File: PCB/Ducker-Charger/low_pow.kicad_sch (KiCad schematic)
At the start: 54 parts, among them IC1 STUSB4710AQ1TR, J3 Conn_01x02, J4 USB_A, J5 USB_A, Q10 AO3400A, Q11 AO3400A, Q6 AO4407A, Q7 AO3400A, Q8 AO4407A, Q9 AO3400A, U3 STPD01PUR, U4 TPS54302, U5 INA3221, U6 TPS54302

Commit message: feat: updated footprints
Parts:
- C16, C17, C18, C19, C21, C22, C23, C25, C26, C27, CCDC1, Cin1, Cout1, Cout2: footprint (none) -> Capacitor_SMD:C_0805_2012Metric
- C20, C24, CBOOT1: footprint (none) -> Capacitor_SMD:C_0603_1608Metric
- IC1: footprint QFN50P300X300X65-16N -> Package_DFN_QFN:QFN-16-1EP_3x3mm_P0.5mm_EP1.7x1.7mm
- J4, J5: footprint (none) -> Connector_USB:USB_A_Molex_67643_Horizontal
- L2: footprint (none) -> Inductor_SMD:L_6.3x6.3_H3
- L3, L4: footprint (none) -> Inductor_SMD:L_7.3x7.3_H4.5
- R12, R13, R14, R15, R16, R17, R18, R19, R20, R21, R22, R23, R24, R25, RCDC1, Ron1, Rshunt1, Rshunt2, Rsns1: footprint (none) -> Resistor_SMD:R_0603_1608Metric
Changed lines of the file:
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@@
 			)
 		)
-		(property "Footprint" ""
+		(property "Footprint" "Resistor_SMD:R_0603_1608Metric"
 			(at 207.518 102.87 90)
 			(effects
@@
 			)
 		)
-		(property "Footprint" ""
+		(property "Footprint" "Resistor_SMD:R_0603_1608Metric"
 			(at 121.92 180.848 90)
 			(effects
@@
 			)
 		)
-		(property "Footprint" ""
+		(property "Footprint" "Resistor_SMD:R_0603_1608Metric"
 			(at 196.85 109.728 90)
 			(effects
@@
 			)
 		)
-		(property "Footprint" ""
+		(property "Footprint" "Capacitor_SMD:C_0805_2012Metric"
 			(at 270.2052 96.52 0)
 			(effects
@@
 			)
 		)
-		(property "Footprint" ""
+		(property "Footprint" "Capacitor_SMD:C_0805_2012Metric"
 			(at 277.8252 218.44 0)
 			(effects
@@
 			)
 		)
-		(property "Footprint" ""
+		(property "Footprint" "Resistor_SMD:R_0603_1608Metric"
 			(at 328.93 212.598 90)
 			(effects
@@
 			)
 		)
-		(property "Footprint" ""
+		(property "Footprint" "Inductor_SMD:L_7.3x7.3_H4.5"
 			(at 269.24 179.07 0)
 			(effects
@@
 			)
 		)
-		(property "Footprint" ""
+		(property "Footprint" "Capacitor_SMD:C_0805_2012Metric"
 			(at 204.1652 217.17 0)
 			(effects
@@
 			)
 		)
-		(property "Footprint" ""
+		(property "Footprint" "Connector_USB:USB_A_Molex_67643_Horizontal"
 			(at 350.52 217.17 0)
 			(effects
@@
 			)
 		)
-		(property "Footprint" ""
+		(property "Footprint" "Capacitor_SMD:C_0805_2012Metric"
 			(at 287.9852 186.69 0)
 			(effects
@@
 			)
 		)
-		(property "Footprint" ""
+		(property "Footprint" "Capacitor_SMD:C_0805_2012Metric"
 			(at 58.1152 80.01 0)
 			(effects
@@
 			)
 		)
-		(property "Footprint" ""
+		(property "Footprint" "Capacitor_SMD:C_0805_2012Metric"
 			(at 117.8052 77.47 0)
 			(effects
@@
 			)
 		)
-		(property "Footprint" ""
+		(property "Footprint" "Capacitor_SMD:C_0603_1608Metric"
 			(at 260.0452 210.82 0)
 			(effects
@@
 			)
 		)
-		(property "Footprint" ""
+		(property "Footprint" "Capacitor_SMD:C_0805_2012Metric"
 			(at 258.7752 96.52 0)
 			(effects
@@
 			)
 		)
-		(property "Footprint" ""
+		(property "Footprint" "Capacitor_SMD:C_0603_1608Metric"
 			(at 100.0252 82.55 0)
 			(effects
@@
 			)
 		)
-		(property "Footprint" ""
+		(property "Footprint" "Resistor_SMD:R_0603_1608Metric"
 			(at 196.85 74.168 90)
 			(effects
@@
 			)
 		)
-		(property "Footprint" ""
+		(property "Footprint" "Capacitor_SMD:C_0805_2012Metric"
 			(at 202.8952 185.42 0)
 			(effects
@@
 			)
 		)
-		(property "Footprint" ""
+		(property "Footprint" "Resistor_SMD:R_0603_1608Metric"
 			(at 99.06 74.168 90)
 			(effects
@@
 			)
 		)
-		(property "Footprint" ""
+		(property "Footprint" "Resistor_SMD:R_0603_1608Metric"
 			(at 327.66 180.848 90)
 			(effects
@@
 			)
 		)
-		(property "Footprint" ""
+		(property "Footprint" "Resistor_SMD:R_0603_1608Metric"
 			(at 123.19 212.598 90)
 			(effects
@@
 			)
 		)
-		(property "Footprint" ""
+		(property "Footprint" "Capacitor_SMD:C_0805_2012Metric"
 			(at 289.2552 218.44 0)
 			(effects
@@
 			)
 		)
-		(property "Footprint" ""
+		(property "Footprint" "Connector_USB:USB_A_Molex_67643_Horizontal"
 			(at 349.25 185.42 0)
 			(effects
@@
 			)
 		)
-		(property "Footprint" ""
+		(property "Footprint" "Resistor_SMD:R_0603_1608Metric"
 			(at 132.842 66.04 90)
 			(effects
@@
 			)
 		)
-		(property "Footprint" ""
+		(property "Footprint" "Resistor_SMD:R_0603_1608Metric"
 			(at 128.778 184.15 90)
 			(effects
@@
 			)
 		)
-		(property "Footprint" ""
+		(property "Footprint" "Resistor_SMD:R_0603_1608Metric"
 			(at 316.23 62.738 90)
 			(effects
@@
 			)
 		)
-		(property "Footprint" ""
+		(property "Footprint" "Resistor_SMD:R_0603_1608Metric"
 			(at 207.518 67.31 90)
 			(effects
@@
 			)
 		)
-		(property "Footprint" ""
+		(property "Footprint" "Capacitor_SMD:C_0805_2012Metric"
 			(at 144.4752 69.85 0)
 			(effects
@@
 			)
 		)
-		(property "Footprint" ""
+		(property "Footprint" "Resistor_SMD:R_0603_1608Metric"
 			(at 127 84.328 90)
 			(effects
@@
 			)
 		)
-		(property "Footprint" ""
+		(property "Footprint" "Resistor_SMD:R_0603_1608Metric"
 			(at 295.402 194.31 90)
 			(effects
@@
 			)
 		)
-		(property "Footprint" ""
+		(property "Footprint" "Resistor_SMD:R_0603_1608Metric"
 			(at 296.672 214.63 90)
 			(effects
@@
 			)
 		)
-		(property "Footprint" ""
+		(property "Footprint" "Inductor_SMD:L_6.3x6.3_H3"
 			(at 106.68 82.55 0)
 			(effects
@@
 			)
 		)
-		(property "Footprint" ""
+		(property "Footprint" "Resistor_SMD:R_0603_1608Metric"
 			(at 295.402 182.88 90)
 			(effects
@@
 			)
 		)
-		(property "Footprint" ""
+		(property "Footprint" "Capacitor_SMD:C_0603_1608Metric"
 			(at 258.7752 179.07 0)
 			(effects
@@
 			)
 		)
-		(property "Footprint" ""
+		(property "Footprint" "Capacitor_SMD:C_0805_2012Metric"
 			(at 35.8648 74.93 0)
 			(effects
@@
 			)
 		)
-		(property "Footprint" ""
+		(property "Footprint" "Capacitor_SMD:C_0805_2012Metric"
 			(at 115.2652 90.17 0)
 			(effects
@@
 			)
 		)
-		(property "Footprint" ""
+		(property "Footprint" "Resistor_SMD:R_0603_1608Metric"
 			(at 316.23 65.278 90)
 			(effects
@@
 			)
 		)
-		(property "Footprint" ""
+		(property "Footprint" "Resistor_SMD:R_0603_1608Metric"
 			(at 130.048 215.9 90)
 			(effects
@@
 			)
 		)
-		(property "Footprint" ""
+		(property "Footprint" "Inductor_SMD:L_7.3x7.3_H4.5"
 			(at 270.51 210.82 0)
 			(effects
@@
 			)
 		)
-		(property "Footprint" ""
+		(property "Footprint" "Capacitor_SMD:C_0805_2012Metric"
 			(at 276.5552 186.69 0)
 			(effects
@@
 			)
 		)
-		(property "Footprint" ""
+		(property "Footprint" "Capacitor_SMD:C_0805_2012Metric"
 			(at 139.3952 90.17 0)
 			(effects
@@
 			)
 		)
-		(property "Footprint" "QFN50P300X300X65-16N"
+		(property "Footprint" "Package_DFN_QFN:QFN-16-1EP_3x3mm_P0.5mm_EP1.7x1.7mm"
 			(at 306.07 150.8 0)
 			(effects
@@
 			)
 		)
-		(property "Footprint" ""
+		(property "Footprint" "Resistor_SMD:R_0603_1608Metric"
 			(at 296.672 226.06 90)
 			(effects

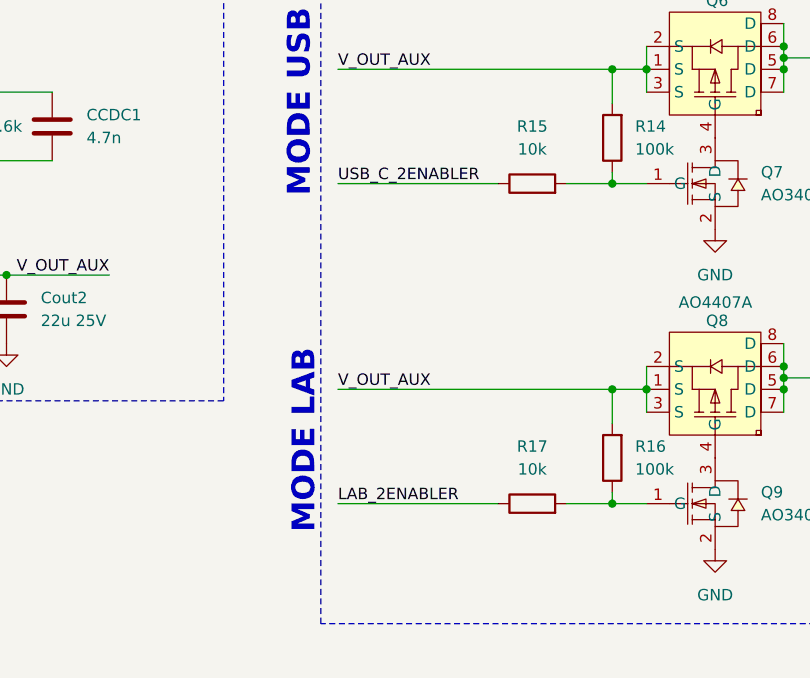
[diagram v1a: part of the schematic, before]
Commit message: fix: updated config based on CubeMX
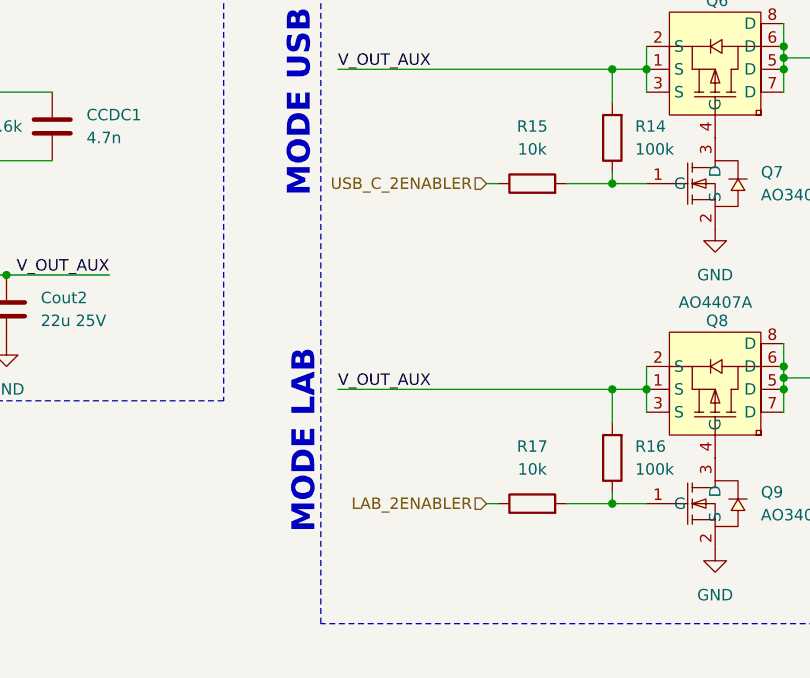
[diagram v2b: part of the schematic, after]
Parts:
- Rsns1: footprint Resistor_SMD:R_0603_1608Metric -> Resistor_SMD:R_1206_3216Metric
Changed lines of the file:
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@@
 	(wire
 		(pts
-			(xy 44.45 274.32) (xy 58.42 274.32)
+			(xy 191.77 107.95) (xy 193.04 107.95)
 		)
 		(stroke
@@
 	(wire
 		(pts
-			(xy 52.07 59.69) (xy 64.77 59.69)
+			(xy 44.45 274.32) (xy 58.42 274.32)
 		)
 		(stroke
@@
 	(wire
 		(pts
-			(xy 236.22 93.98) (xy 224.79 93.98)
+			(xy 52.07 59.69) (xy 64.77 59.69)
 		)
 		(stroke
@@
 	(wire
 		(pts
-			(xy 175.26 72.39) (xy 193.04 72.39)
+			(xy 236.22 93.98) (xy 224.79 93.98)
 		)
 		(stroke
@@
 	(wire
 		(pts
+			(xy 191.77 72.39) (xy 193.04 72.39)
+		)
+		(stroke
+			(width 0)
+			(type default)
+		)
+	)
+	(wire
+		(pts
 			(xy 359.41 81.28) (xy 370.84 81.28)
 		)
@@
 	(wire
 		(pts
-			(xy 175.26 107.95) (xy 193.04 107.95)
-		)
-		(stroke
-			(width 0)
-			(type default)
-		)
-	)
-	(wire
-		(pts
 			(xy 175.26 59.69) (xy 205.74 59.69)
 		)
@@
 		)
 	)
-	(label "LAB_2ENABLER"
-		(at 175.26 107.95 0)
-		(effects
-			(font
-				(size 1.27 1.27)
-			)
-			(justify left bottom)
-		)
-	)
 	(label "USB_A1_FB"
 		(at 309.88 187.96 180)
@@
 		)
 	)
-	(label "USB_C_2ENABLER"
-		(at 175.26 72.39 0)
-		(effects
-			(font
-				(size 1.27 1.27)
-			)
-			(justify left bottom)
-		)
-	)
 	(label "I2C_LP.SDA"
 		(at 86.36 200.66 180)
@@
 		)
 	)
+	(hierarchical_label "USB_C_2ENABLER"
+		(shape input)
+		(at 191.77 72.39 180)
+		(effects
+			(font
+				(size 1.27 1.27)
+			)
+			(justify right)
+		)
+	)
+	(hierarchical_label "LAB_2ENABLER"
+		(shape input)
+		(at 191.77 107.95 180)
+		(effects
+			(font
+				(size 1.27 1.27)
+			)
+			(justify right)
+		)
+	)
 	(symbol
 		(lib_id "power:GND")
@@
 			)
 		)
-		(property "Footprint" "Resistor_SMD:R_0603_1608Metric"
+		(property "Footprint" "Resistor_SMD:R_1206_3216Metric"
 			(at 127 84.328 90)
 			(effects

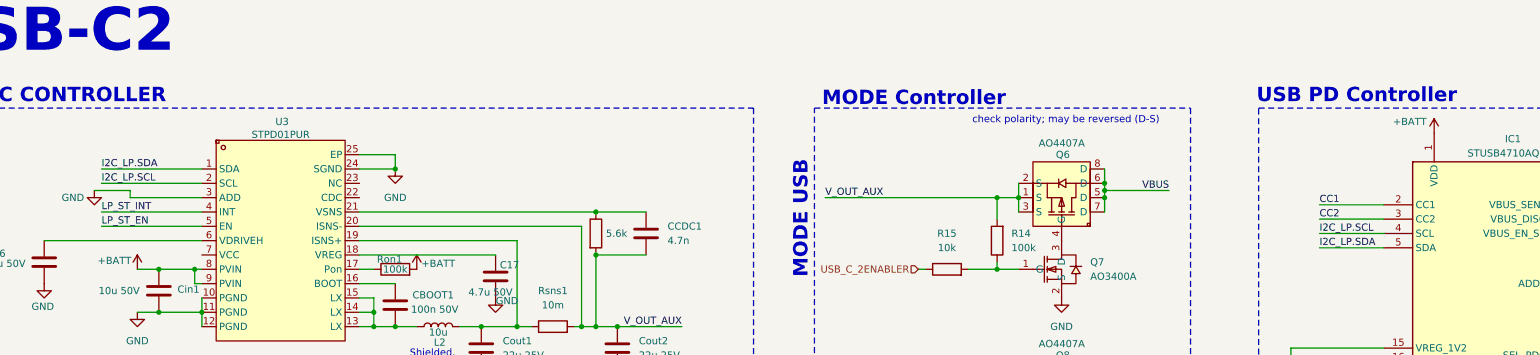
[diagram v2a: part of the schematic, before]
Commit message: fix: added missing connections
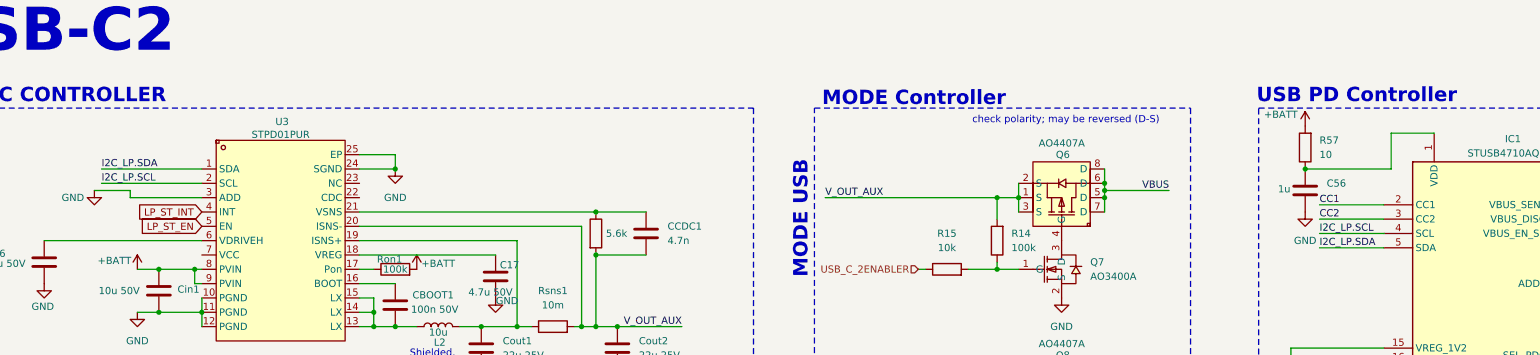
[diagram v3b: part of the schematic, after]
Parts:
- added C56: 1u, Capacitor_SMD:C_0603_1608Metric, symbol Device:C
- added R57: 10, Resistor_SMD:R_0603_1608Metric, symbol Device:R
- Rshunt1, Rshunt2: footprint Resistor_SMD:R_0603_1608Metric -> Resistor_SMD:R_1206_3216Metric
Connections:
- net +BATT: now also R57.2; no longer IC1.1 (VDD)
- net GND: now also C56.2
- new net: C56.1, IC1.1 (VDD), R57.1

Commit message: feat: remade the PCB & minor schematic fixes
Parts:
- added D301: USBLC6-4SC6, EasyEDA:SOT-23-6_L2.9-W1.6-P0.95-LS2.8-BL, symbol EasyEDA:USBLC6-4SC6
- added R309, R310, RCDC301: 10k, Resistor_SMD:R_0603_1608Metric, symbol Device:R
- C303: renamed from C21; value 10u -> 10u 25V; footprint Capacitor_SMD:C_0805_2012Metric -> Capacitor_SMD:C_1206_3216Metric
- C304: renamed from C25; value 10u -> 10u 25V; footprint Capacitor_SMD:C_0805_2012Metric -> Capacitor_SMD:C_1206_3216Metric
- Cout301: renamed from Cout1; value 22u 25V -> 22u 35V; footprint Capacitor_SMD:C_0805_2012Metric -> Capacitor_SMD:C_1210_3225Metric
- Cout302: renamed from Cout2; value 22u 25V -> 22u 35V; footprint Capacitor_SMD:C_0805_2012Metric -> Capacitor_SMD:C_1210_3225Metric
- J303: renamed from J3; footprint (none) -> TerminalBlock:TerminalBlock_bornier-2_P5.08mm
- L301: renamed from L2; value 10u -> 10u 5A; footprint Inductor_SMD:L_6.3x6.3_H3 -> Inductor_SMD:L_7.3x7.3_H4.5
- Rsns301: renamed from Rsns1; value 10m -> 25m
- renumbered C16 to C301, C17 to C302, C18 to C305, C20 to C306, C24 to C307, C56 to C308, C19 to C309, C22 to C310, C26 to C311, C23 to C312, C27 to C313, CBOOT1 to CBOOT301, CCDC1 to CCDC301, Cin1 to Cin301, IC1 to IC301, J4 to J301, J5 to J302, L3 to L302, L4 to L303, Q10 to Q301, Q11 to Q302, Q7 to Q303, Q9 to Q304, Q6 to Q305, Q8 to Q306, R18 to R301, R22 to R302, R20 to R303, R24 to R304, R15 to R305, R17 to R306, R14 to R307, R16 to R308, R57 to R311, R19 to R312, R21 to R313, R23 to R314, R25 to R315, R12 to R316, R13 to R317, RCDC1 to RCDC302, Ron1 to Ron301, Rshunt1 to Rshunt301, Rshunt2 to Rshunt302, U5 to U301, U3 to U302, U4 to U303, U6 to U304, USBC2 to USBC301
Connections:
- net +3V3: now also R309.1, R310.1
- net +BATT: now also U302.7 (VCC); no longer Ron301.2
- net CC1: now also D301.4
- net CC2: now also D301.6
- net DN: now also D301.3
- net DP: now also D301.1
- net GND: now also U301.1 (IN-3), U301.2 (IN+3), D301.2, RCDC301.2
- net USB_A1_EN: now also R309.2
- net USB_A2_EN: now also R310.2
- net VBUS: now also D301.5
- net at U302.22 (CDC): now also RCDC301.1
- net C2_RDY renamed C2.RDY
- net LAB_2ENABLER renamed C2.LAB_EN
- net LP_ST_EN renamed C2.ST_EN
- net LP_ST_INT renamed C2.ST_INT
- net USB_A1_CTRL renamed USBA.1_CTRL
- net USB_A2_CTRL renamed USBA.2_CTRL
- net USB_C_2ENABLER renamed C2.PORT_EN
- new net +5V: Ron301.2
- no-connect marks 4 -> 12
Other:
- note added: "ESD PROTECTION"
- moved on the sheet: C301, C302, C305, C308, C309, CBOOT301, CCDC301, Cin301, Cout301, Cout302, IC301, J303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

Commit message: feat: final version before prod
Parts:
- removed IC301: STUSB4710AQ1TR, Package_DFN_QFN:QFN-16-1EP_3x3mm_P0.5mm_EP1.7x1.7mm, symbol STUSB4710AQ1TR:STUSB4710AQ1TR
- removed R317: 50, Resistor_SMD:R_0603_1608Metric, symbol Device:R
- added C314: 1u, Resistor_SMD:R_0603_1608Metric, symbol Device:C
- added C327: 2.2u, Capacitor_SMD:C_0805_2012Metric, symbol Device:C
- added C391: 100n, Resistor_SMD:R_0603_1608Metric, symbol Device:C
- added D302: LED, LED_SMD:LED_0603_1608Metric, symbol Device:LED
- added IC302: CYPD3175-24LQXQ, QFN50P400X400X60-25N-D, symbol LIB_CYPD3175-24LQXQ:CYPD3175-24LQXQ
- added J304: Debug, Eagle_Connectors:SAMTEC_FTSH-107-01-L-DV-K-TR, symbol Connector:Conn_ST_STDC14
- added R318: 1k, Resistor_SMD:R_0603_1608Metric, symbol Device:R
- C305: value 1u -> 390p; footprint Capacitor_SMD:C_0805_2012Metric -> Resistor_SMD:R_0603_1608Metric
- C308: value 1u -> 390p; footprint Capacitor_SMD:C_0603_1608Metric -> Resistor_SMD:R_0603_1608Metric
- C309: value 1u -> 100n; footprint Capacitor_SMD:C_0805_2012Metric -> Resistor_SMD:R_0603_1608Metric
- R311: value 10 -> 200k
- R316: value 1k2 -> 63k
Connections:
- net +3V3: now also C327.1, C391.1, IC302.23 (VDDD), J304.3 (VCC)
- net +BATT: no longer R311.2
- net C2.RDY: now also IC302.10 (GPIO_3)
- net CC1: now also C305.1, IC302.15 (CC1)
- net CC2: now also C308.1, IC302.14 (CC2)
- net GND: now also R316.2, C314.2, C327.2, C391.2, D302.1 (K), IC302.22 (GND), IC302.25 (EPAD), J304.11 (GNDDetect), J304.5 (GND), J304.7 (GND)
- net I2C_LP.SCL: now also IC302.13 (GPIO_20VT_2)
- net I2C_LP.SDA: now also IC302.12 (GPIO_20VT_1)
- net VBUS: now also R311.1, IC302.11 (VBUS_C_MON_DISCH), IC302.19 (CSP); no longer R316.2
- net at C309.1: now also IC302.21 (CATH/COMP)
- net at R316.1: now also R311.2, IC302.20 (FB)
- new net: D302.2 (A), R318.2
- new net: C314.1, IC302.24 (VCCD)
- new net: IC302.2 (GPIO_2), R318.1
- new net SWCLK: IC302.8 (SWD_CLK_0/GPIO), J304.6 (JCLK/SWCLK)
- new net SWDIO: IC302.7 (SWD_DAT_0/GPIO), J304.4 (JTMS/SWDIO)
- new net ~{RESET}: IC302.9 (AXRES/GPIO), J304.12 (~{RST})
- no-connect marks 12 -> 22
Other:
- note added: "Debug connector"
- moved on the sheet: C301, C302, C303, C304, C306, C307, C310, C311, C312, C313, CBOOT301, CCDC301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
